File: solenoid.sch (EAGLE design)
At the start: 40 parts, among them Y1 ECS-80-S-4X

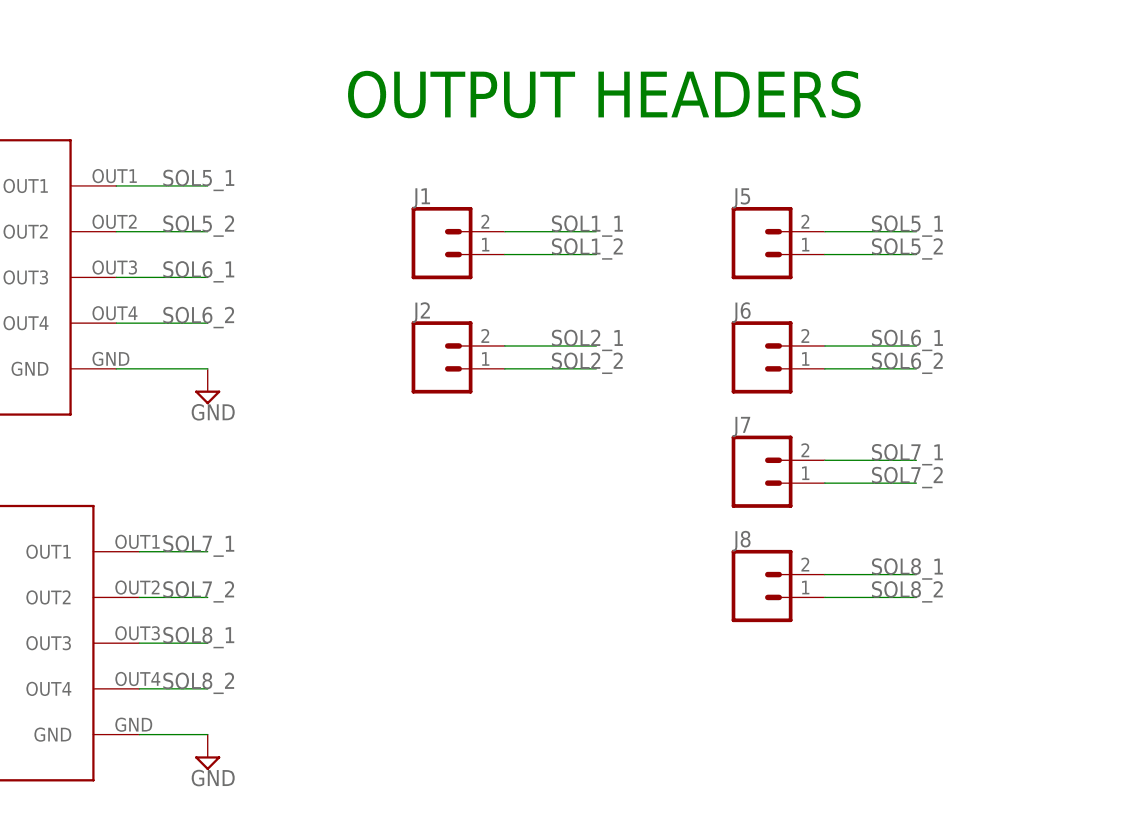
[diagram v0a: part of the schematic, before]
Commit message: added standoff, moved around some header
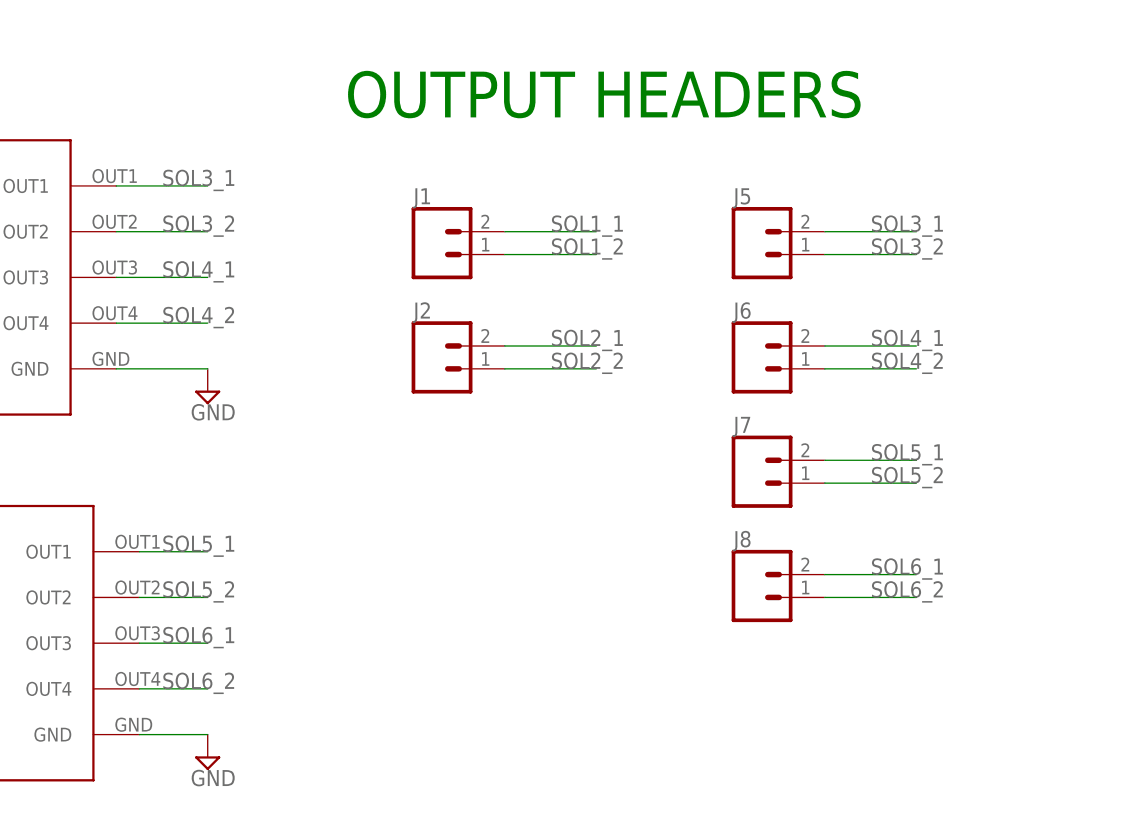
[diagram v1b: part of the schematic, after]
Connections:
- removed net SOL7_1: J7.2, U$6.OUT1
- removed net SOL7_2: J7.1, U$6.OUT2
- removed net SOL8_1: J8.2, U$6.OUT3
- removed net SOL8_2: J8.1, U$6.OUT4
- new net SOL3_1: J5.2, U$5.OUT1
- new net SOL3_2: J5.1, U$5.OUT2
- new net SOL4_1: J6.2, U$5.OUT3
- new net SOL4_2: J6.1, U$5.OUT4
- net SOL5_1: now also J7.2, U$6.OUT1; no longer J5.2, U$5.OUT1
- net SOL5_2: now also J7.1, U$6.OUT2; no longer J5.1, U$5.OUT2
- net SOL6_1: now also J8.2, U$6.OUT3; no longer J6.2, U$5.OUT3
- net SOL6_2: now also J8.1, U$6.OUT4; no longer J6.1, U$5.OUT4

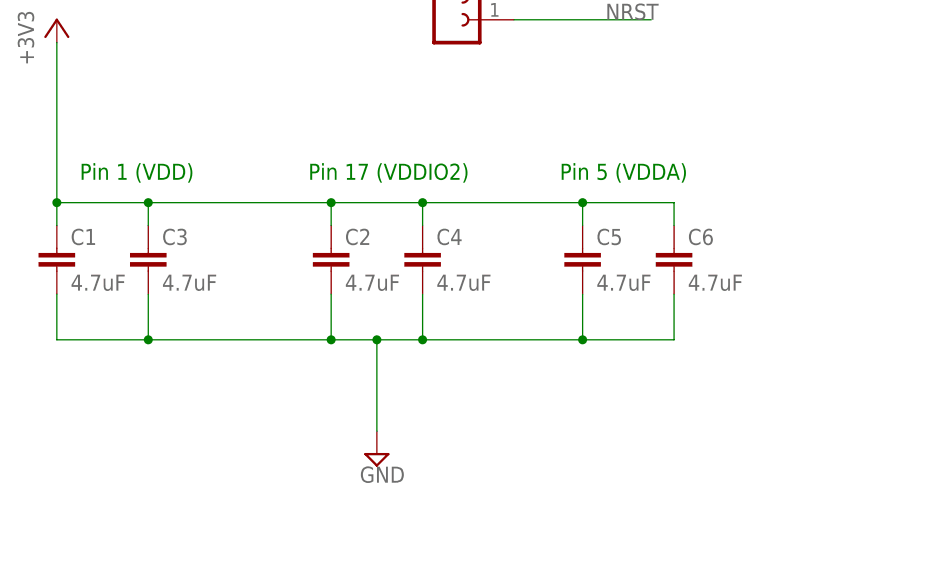
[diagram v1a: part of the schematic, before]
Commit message: Solenoid v1
Final changes to capacitor and few small changes
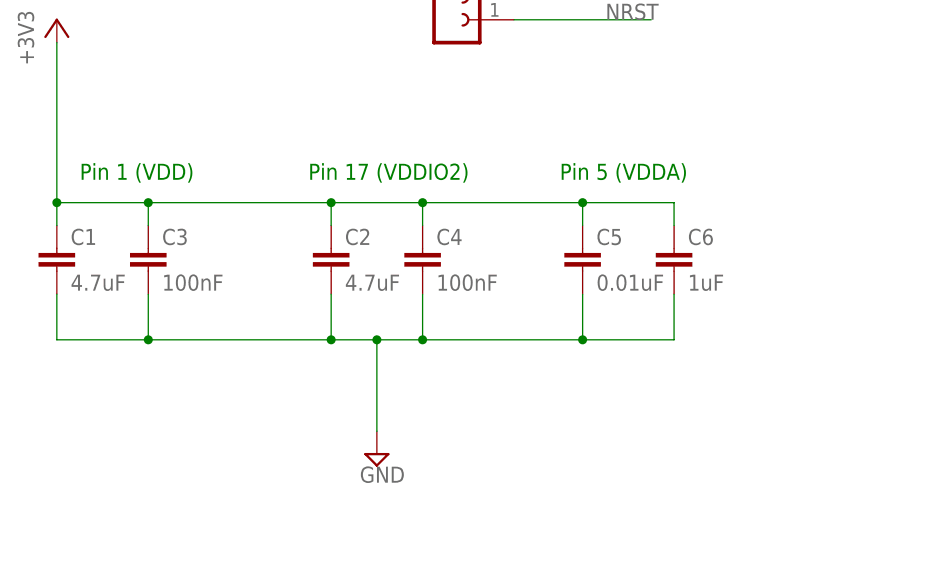
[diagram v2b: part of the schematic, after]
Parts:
- C3, C4: value 4.7uF -> 100nF
- C5: value 4.7uF -> 0.01uF
- C6: value 4.7uF -> 1uF
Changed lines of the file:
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@@
 <?xml version="1.0" encoding="utf-8"?>
 <!DOCTYPE eagle SYSTEM "eagle.dtd">
-<eagle version="9.3.2">
+<eagle version="9.1.3">
 <drawing>
 <settings>
@@
 <part name="C1" library="SparkFun-Capacitors" library_urn="urn:adsk.eagle:library:510" deviceset="4.7UF" device="0603" package3d_urn="urn:adsk.eagle:package:37414/1" value="4.7uF"/>
 <part name="C2" library="SparkFun-Capacitors" library_urn="urn:adsk.eagle:library:510" deviceset="4.7UF" device="0603" package3d_urn="urn:adsk.eagle:package:37414/1" value="4.7uF"/>
-<part name="C3" library="SparkFun-Capacitors" library_urn="urn:adsk.eagle:library:510" deviceset="4.7UF" device="0603" package3d_urn="urn:adsk.eagle:package:37414/1" value="4.7uF"/>
-<part name="C4" library="SparkFun-Capacitors" library_urn="urn:adsk.eagle:library:510" deviceset="4.7UF" device="0603" package3d_urn="urn:adsk.eagle:package:37414/1" value="4.7uF"/>
-<part name="C5" library="SparkFun-Capacitors" library_urn="urn:adsk.eagle:library:510" deviceset="4.7UF" device="0603" package3d_urn="urn:adsk.eagle:package:37414/1" value="4.7uF"/>
-<part name="C6" library="SparkFun-Capacitors" library_urn="urn:adsk.eagle:library:510" deviceset="4.7UF" device="0603" package3d_urn="urn:adsk.eagle:package:37414/1" value="4.7uF"/>
+<part name="C3" library="SparkFun-Capacitors" library_urn="urn:adsk.eagle:library:510" deviceset="4.7UF" device="0603" package3d_urn="urn:adsk.eagle:package:37414/1" value="100nF"/>
+<part name="C4" library="SparkFun-Capacitors" library_urn="urn:adsk.eagle:library:510" deviceset="4.7UF" device="0603" package3d_urn="urn:adsk.eagle:package:37414/1" value="100nF"/>
+<part name="C5" library="SparkFun-Capacitors" library_urn="urn:adsk.eagle:library:510" deviceset="4.7UF" device="0603" package3d_urn="urn:adsk.eagle:package:37414/1" value="0.01uF"/>
+<part name="C6" library="SparkFun-Capacitors" library_urn="urn:adsk.eagle:library:510" deviceset="4.7UF" device="0603" package3d_urn="urn:adsk.eagle:package:37414/1" value="1uF"/>
 <part name="GND" library="supply2" library_urn="urn:adsk.eagle:library:372" deviceset="GND" device=""/>
 <part name="GND1" library="supply2" library_urn="urn:adsk.eagle:library:372" deviceset="GND" device=""/>

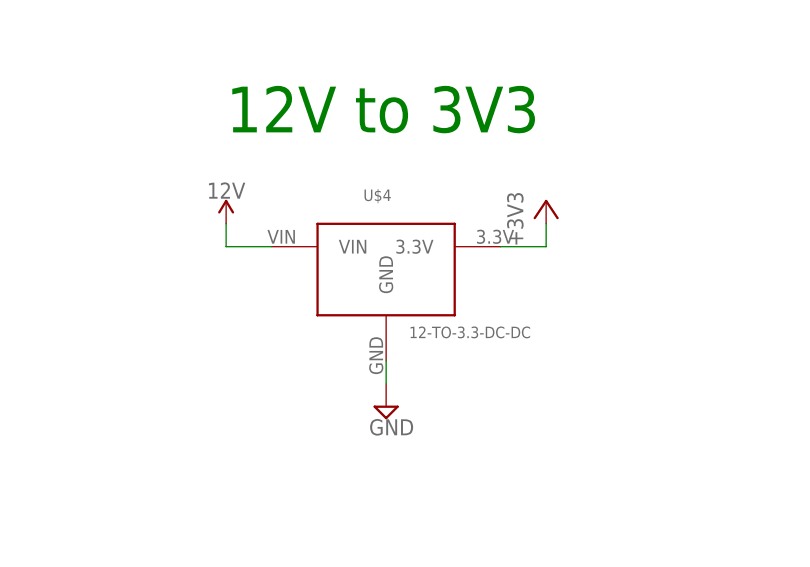
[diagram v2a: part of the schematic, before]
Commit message: Update 12->3.3 converter, make extra layers inactive, fix names
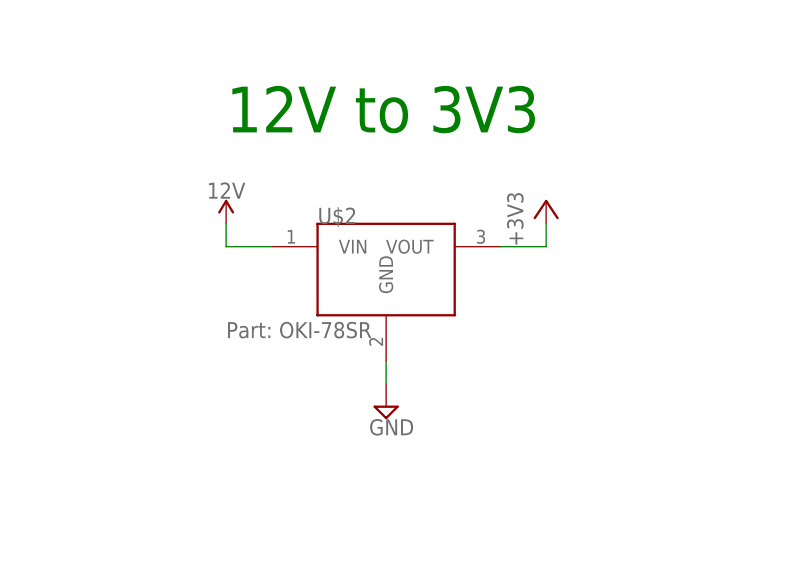
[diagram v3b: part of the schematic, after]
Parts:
- removed U$4: 12-TO-3.3-DC-DC, ece477:12-TO-3.3-DC-DC
- added U$2: MURATA-DC-DC, MURATA_3pin_dcdc:MURATA-DC-DC
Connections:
- net +3V3: now also U$2.VOUT; no longer U$4.3.3V
- net 12V: now also U$2.VIN; no longer U$4.VIN
- net GND: now also U$2.GND; no longer U$4.GND
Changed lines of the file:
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@@
 <?xml version="1.0" encoding="utf-8"?>
 <!DOCTYPE eagle SYSTEM "eagle.dtd">
-<eagle version="9.1.3">
+<eagle version="9.6.2">
 <drawing>
 <settings>
@@
 <part name="R4" library="SparkFun-Resistors" library_urn="urn:adsk.eagle:library:532" deviceset="RESISTOR" device="0603" package3d_urn="urn:adsk.eagle:package:39650@1/1" value=" "/>
 <part name="R6" library="SparkFun-Resistors" library_urn="urn:adsk.eagle:library:532" deviceset="RESISTOR" device="0603" package3d_urn="urn:adsk.eagle:package:39650@1/1" value=" "/>
-<part name="U$4" library="ece477" deviceset="12-TO-3.3-DC-DC" device=""/>
 <part name="+3V5" library="supply1" library_urn="urn:adsk.eagle:library:371" deviceset="+3V3" device=""/>
 <part name="GND6" library="supply2" library_urn="urn:adsk.eagle:library:372" deviceset="GND" device=""/>
@@
 <part name="J3" library="SparkFun-Connectors" library_urn="urn:adsk.eagle:library:513" deviceset="CONN_02" device="" package3d_urn="urn:adsk.eagle:package:38039/1"/>
 <part name="J4" library="SparkFun-Connectors" library_urn="urn:adsk.eagle:library:513" deviceset="CONN_02" device="" package3d_urn="urn:adsk.eagle:package:38039/1"/>
+<part name="U$2" library="MURATA_3pin_dcdc" deviceset="MURATA-DC-DC" device="" package3d_urn="urn:adsk.eagle:package:23169699/2"/>
 </parts>
 <sheets>
@@
 <attribute name="VALUE" x="280.924" y="-43.18" size="1.778" layer="96" font="vector" rot="R90" align="top-center"/>
 </instance>
-<instance part="U$4" gate="A" x="172.72" y="58.42" smashed="yes">
-<attribute name="NAME" x="170.18" y="68.58" size="1.27" layer="95"/>
-<attribute name="VALUE" x="175.26" y="53.34" size="1.27" layer="95"/>
-</instance>
 <instance part="+3V5" gate="G$1" x="190.5" y="68.58" smashed="yes">
 <attribute name="VALUE" x="187.96" y="63.5" size="1.778" layer="96" rot="R90"/>
@@
 <attribute name="NAME" x="396.24" y="-57.912" size="1.778" layer="95" font="vector"/>
 </instance>
+<instance part="U$2" gate="G$1" x="167.64" y="63.5" smashed="yes">
+<attribute name="NAME" x="165.1" y="66.04" size="1.778" layer="95"/>
+</instance>
 </instances>
 <busses>
@@
 </segment>
 <segment>
-<pinref part="U$4" gate="A" pin="GND"/>
 <wire x1="172.72" y1="50.8" x2="172.72" y2="48.26" width="0.1524" layer="91"/>
 <pinref part="GND6" gate="GND" pin="GND"/>
+<pinref part="U$2" gate="G$1" pin="GND"/>
 </segment>
 <segment>
@@
 <segment>
 <pinref part="+3V5" gate="G$1" pin="+3V3"/>
-<pinref part="U$4" gate="A" pin="3.3V"/>
 <wire x1="190.5" y1="66.04" x2="190.5" y2="63.5" width="0.1524" layer="91"/>
 <wire x1="190.5" y1="63.5" x2="185.42" y2="63.5" width="0.1524" layer="91"/>
+<pinref part="U$2" gate="G$1" pin="VOUT"/>
 </segment>
 <segment>
@@
 </segment>
 <segment>
-<pinref part="U$4" gate="A" pin="VIN"/>
 <wire x1="160.02" y1="63.5" x2="154.94" y2="63.5" width="0.1524" layer="91"/>
 <wire x1="154.94" y1="63.5" x2="154.94" y2="66.04" width="0.1524" layer="91"/>
 <pinref part="SUPPLY2" gate="G$1" pin="12V"/>
-</segment>
-<segment>
+<pinref part="U$2" gate="G$1" pin="VIN"/>
+</segment>
+<segment>

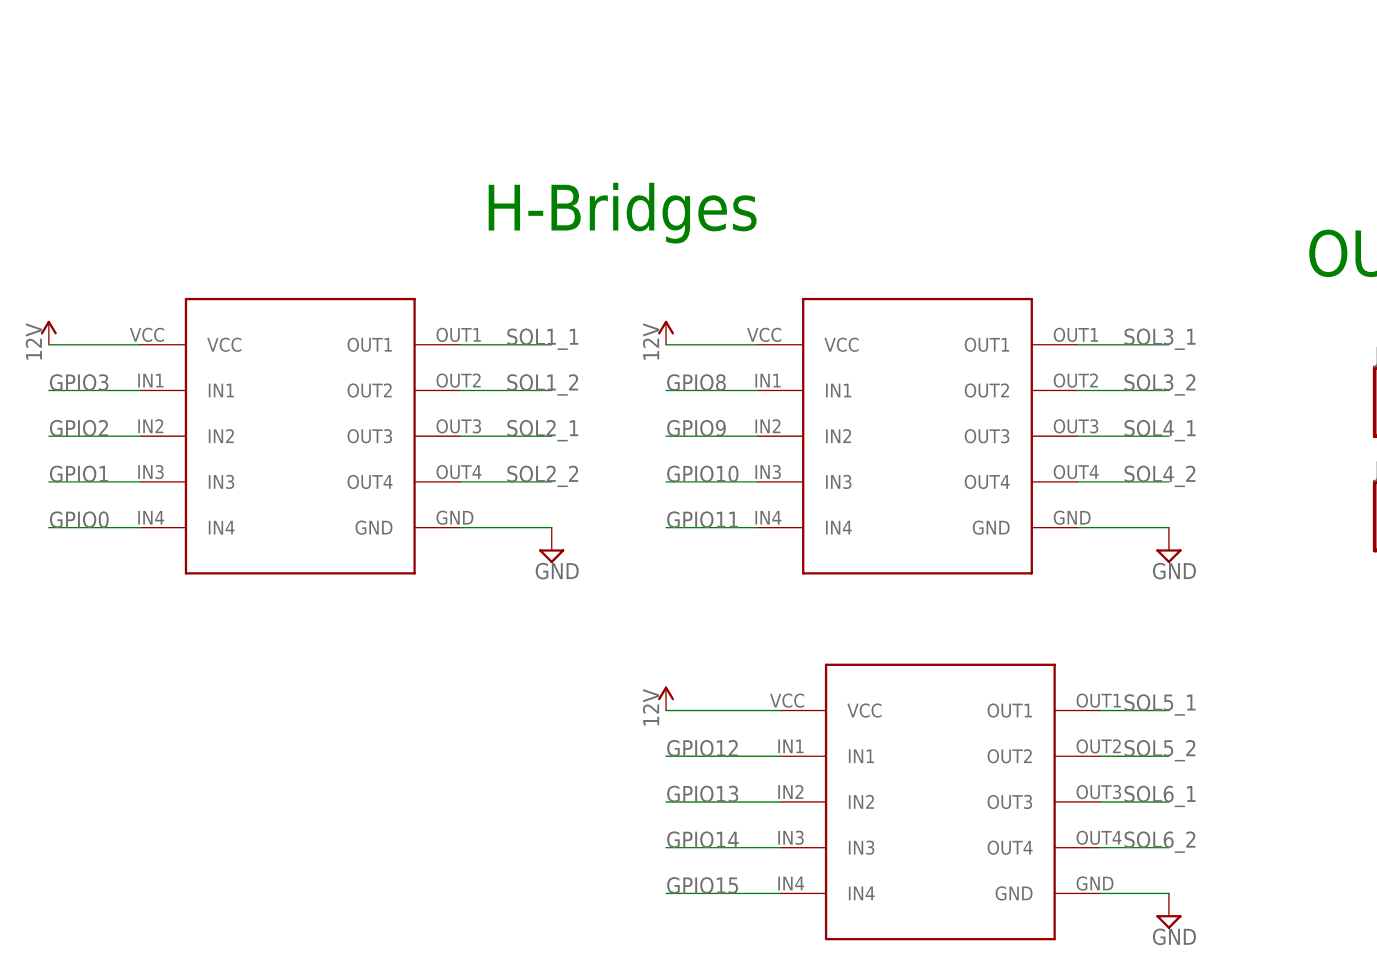
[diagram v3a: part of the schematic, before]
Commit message: deleted h bridges - broken
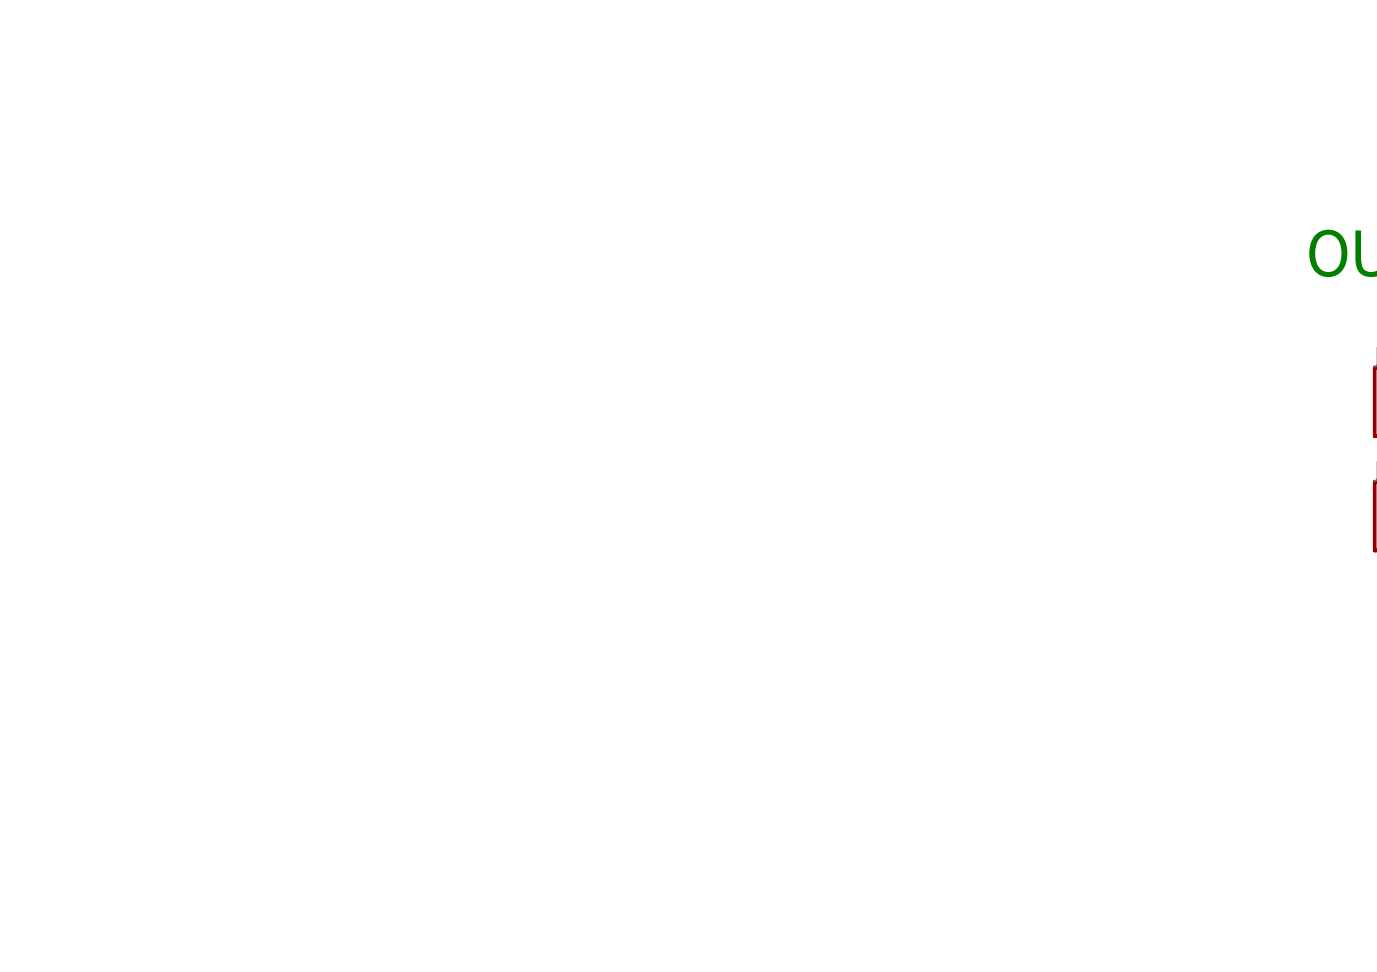
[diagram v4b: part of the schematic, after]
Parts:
- removed U$1, U$5, U$6: LV8548M, HBridge:LV8548M
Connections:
- net 12V: no longer U$1.VCC, U$5.VCC, U$6.VCC
- net GND: no longer U$1.GND, U$5.GND, U$6.GND
- net GPIO0: no longer U$1.IN4
- net GPIO1: no longer U$1.IN3
- net GPIO10: no longer U$5.IN3
- net GPIO11: no longer U$5.IN4
- net GPIO12: no longer U$6.IN1
- net GPIO13: no longer U$6.IN2
- net GPIO14: no longer U$6.IN3
- net GPIO15: no longer U$6.IN4
- net GPIO2: no longer U$1.IN2
- net GPIO3: no longer U$1.IN1
- net GPIO8: no longer U$5.IN1
- net GPIO9: no longer U$5.IN2
- net SOL1_1: no longer U$1.OUT1
- net SOL1_2: no longer U$1.OUT2
- net SOL2_1: no longer U$1.OUT3
- net SOL2_2: no longer U$1.OUT4
- net SOL3_1: no longer U$5.OUT1
- net SOL3_2: no longer U$5.OUT2
- net SOL4_1: no longer U$5.OUT3
- net SOL4_2: no longer U$5.OUT4
- net SOL5_1: no longer U$6.OUT1
- net SOL5_2: no longer U$6.OUT2
- net SOL6_1: no longer U$6.OUT3
- net SOL6_2: no longer U$6.OUT4
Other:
- note removed: "H-Bridges"
